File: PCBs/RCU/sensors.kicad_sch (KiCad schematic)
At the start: 11 parts, among them U501 LSM6DS3

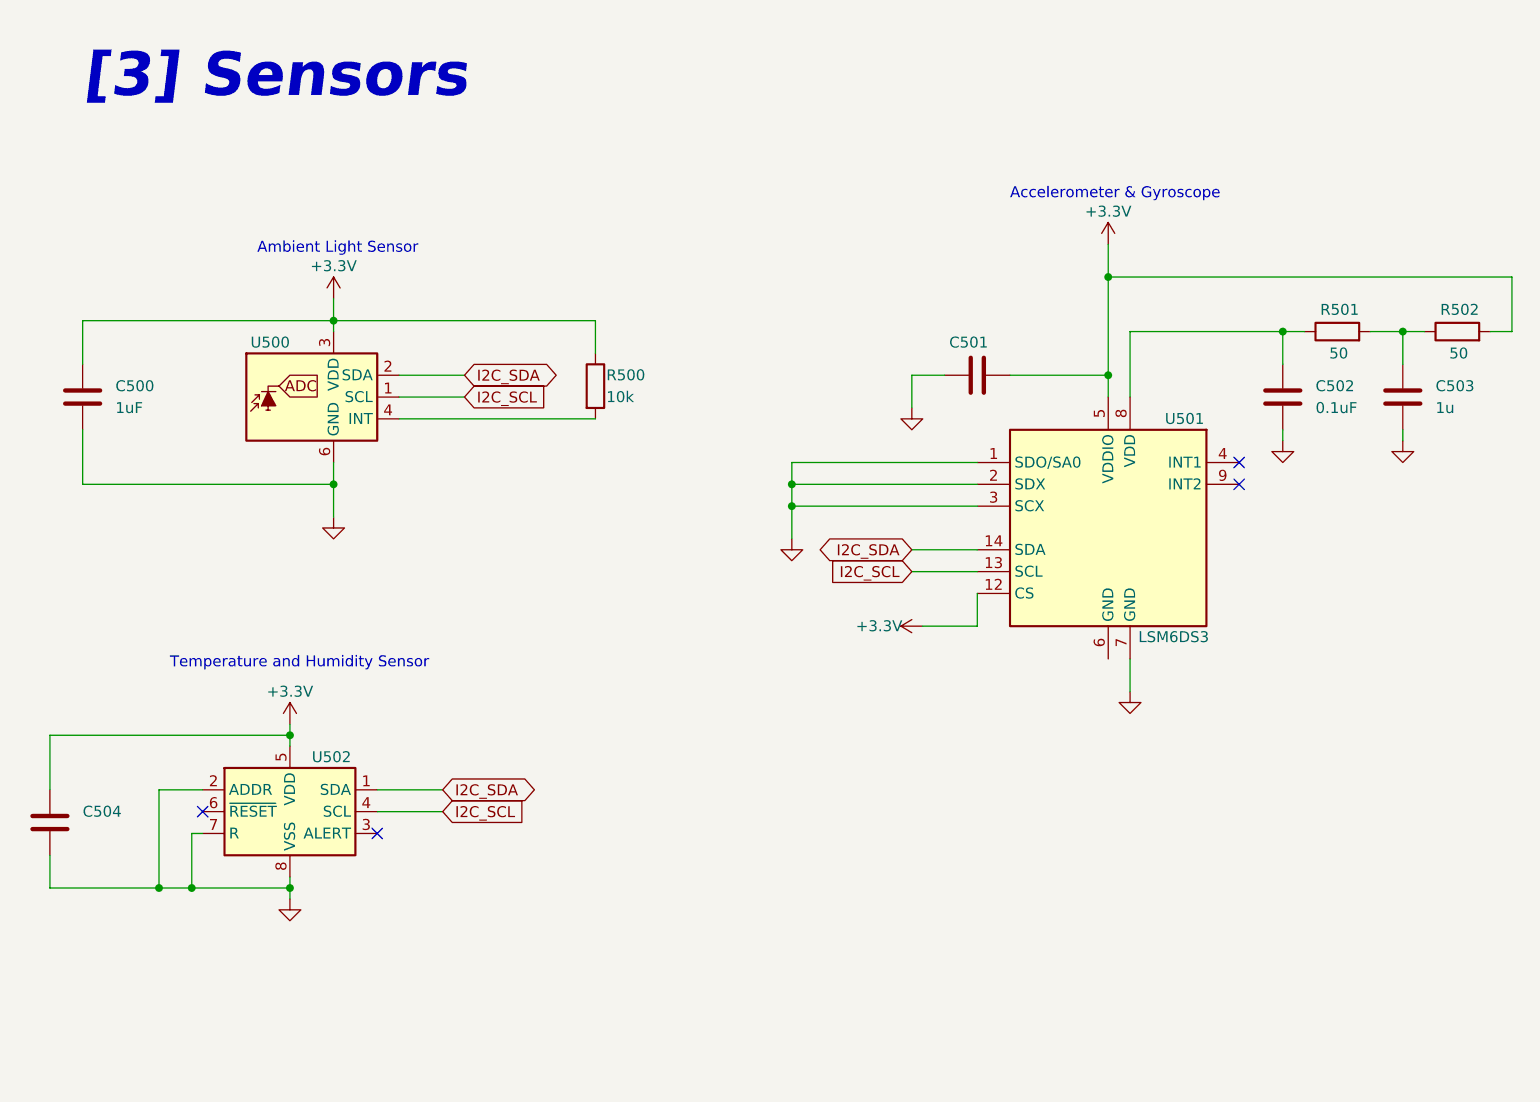
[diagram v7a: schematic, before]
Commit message: Sectioned ADC module and corrected Motor current output name
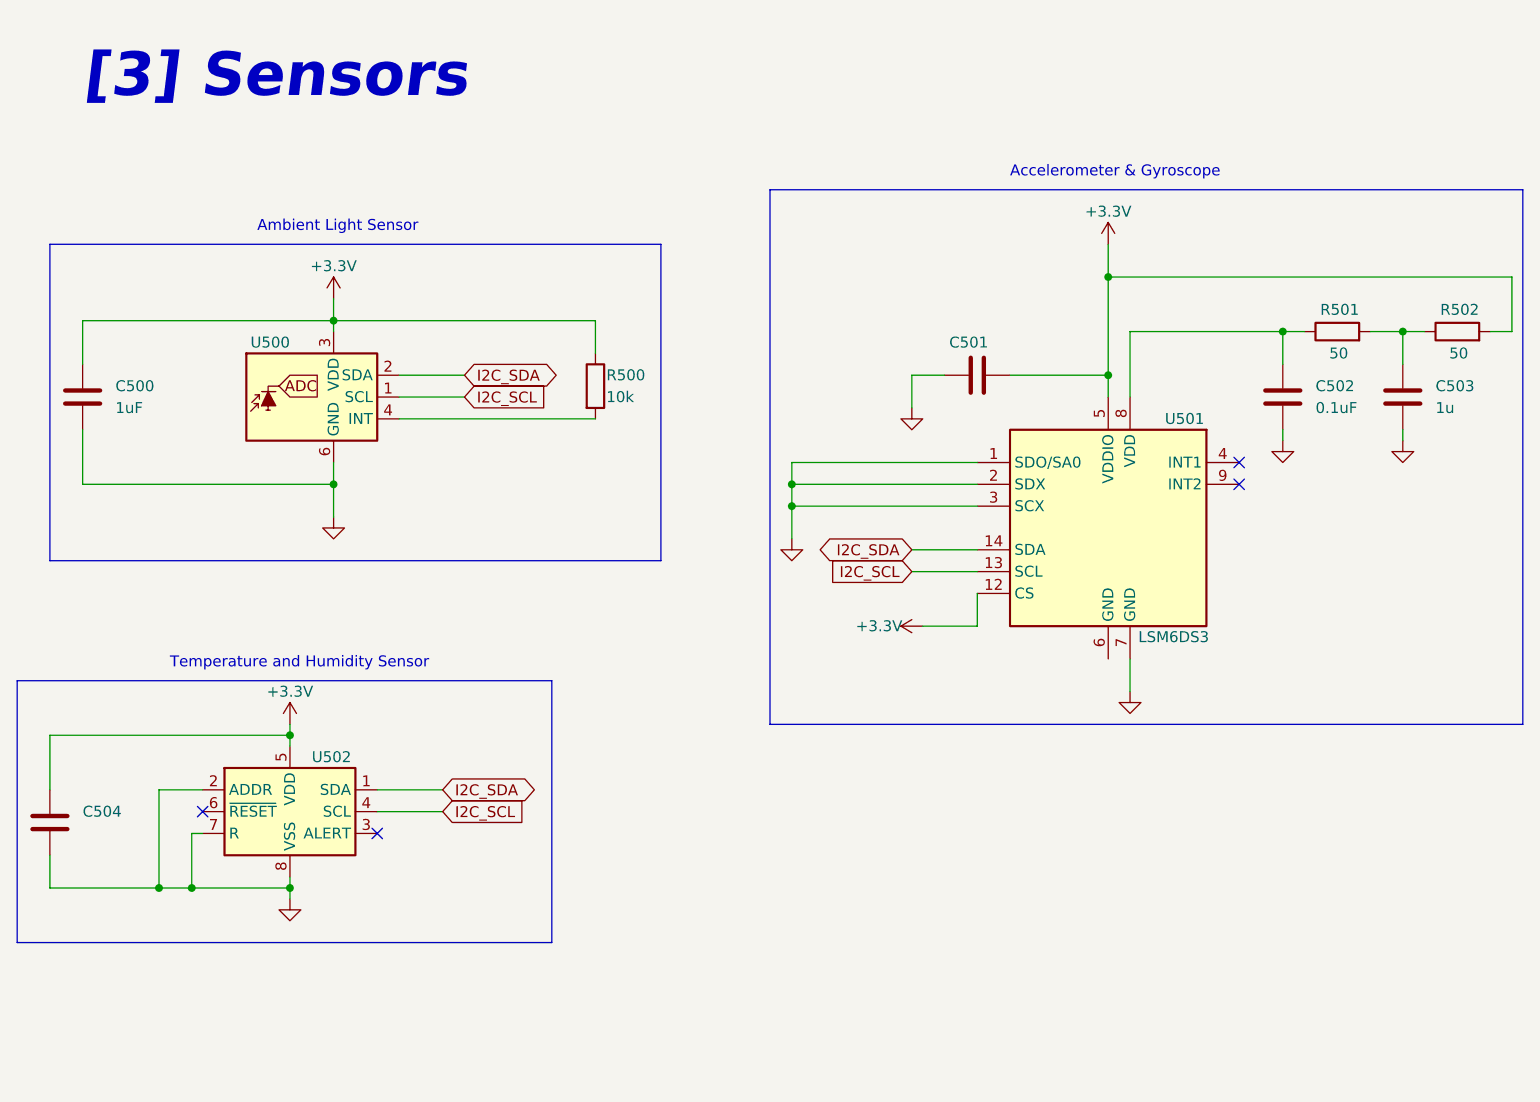
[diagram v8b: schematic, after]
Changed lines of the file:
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@@
+    (stroke (width 0) (type default) (color 0 0 0 0))
+  )
+  (polyline (pts (xy 88.9 81.28) (xy 88.9 44.45))
     (stroke (width 0) (type default) (color 0 0 0 0))
   )
@@
     (stroke (width 0) (type default) (color 0 0 0 0))
   )
+  (polyline (pts (xy 13.97 125.73) (xy 13.97 95.25))
+    (stroke (width 0) (type default) (color 0 0 0 0))
+  )
+  (polyline (pts (xy 76.2 125.73) (xy 13.97 125.73))
+    (stroke (width 0) (type default) (color 0 0 0 0))
+  )
+  (polyline (pts (xy 88.9 44.45) (xy 17.78 44.45))
+    (stroke (width 0) (type default) (color 0 0 0 0))
+  )
   (wire (pts (xy 125.73 80.01) (xy 118.11 80.01))
     (stroke (width 0) (type default) (color 0 0 0 0))
@@
     (stroke (width 0) (type default) (color 0 0 0 0))
   )
+  (polyline (pts (xy 17.78 44.45) (xy 17.78 81.28))
+    (stroke (width 0) (type default) (color 0 0 0 0))
+  )
+  (polyline (pts (xy 189.23 38.1) (xy 189.23 100.33))
+    (stroke (width 0) (type default) (color 0 0 0 0))
+  )
   (wire (pts (xy 187.96 54.61) (xy 187.96 48.26))
     (stroke (width 0) (type default) (color 0 0 0 0))
@@
     (stroke (width 0) (type default) (color 0 0 0 0))
   )
+  (polyline (pts (xy 101.6 100.33) (xy 101.6 38.1))
+    (stroke (width 0) (type default) (color 0 0 0 0))
+  )
   (wire (pts (xy 185.42 54.61) (xy 187.96 54.61))
     (stroke (width 0) (type default) (color 0 0 0 0))
@@
     (stroke (width 0) (type default) (color 0 0 0 0))
   )
+  (polyline (pts (xy 17.78 81.28) (xy 88.9 81.28))
+    (stroke (width 0) (type default) (color 0 0 0 0))
+  )
   (wire (pts (xy 118.11 59.69) (xy 121.92 59.69))
     (stroke (width 0) (type default) (color 0 0 0 0))
   )
+  (polyline (pts (xy 76.2 95.25) (xy 76.2 125.73))
+    (stroke (width 0) (type default) (color 0 0 0 0))
+  )
   (wire (pts (xy 118.11 59.69) (xy 118.11 63.5))
     (stroke (width 0) (type default) (color 0 0 0 0))
   )
+  (polyline (pts (xy 101.6 38.1) (xy 189.23 38.1))
+    (stroke (width 0) (type default) (color 0 0 0 0))
+  )
   (wire (pts (xy 45.72 100.33) (xy 45.72 101.6))
     (stroke (width 0) (type default) (color 0 0 0 0))
@@
     (stroke (width 0) (type default) (color 0 0 0 0))
   )
+  (polyline (pts (xy 189.23 100.33) (xy 101.6 100.33))
+    (stroke (width 0) (type default) (color 0 0 0 0))
+  )
   (wire (pts (xy 140.97 59.69) (xy 129.54 59.69))
     (stroke (width 0) (type default) (color 0 0 0 0))
@@
   )
   (wire (pts (xy 50.8 69.85) (xy 50.8 72.39))
+    (stroke (width 0) (type default) (color 0 0 0 0))
+  )
+  (polyline (pts (xy 13.97 95.25) (xy 76.2 95.25))
     (stroke (width 0) (type default) (color 0 0 0 0))
   )
@@
     (effects (font (size 5.08 5.08) (thickness 1.016) bold italic) (justify left bottom))
   )
-  (text "Accelerometer & Gyroscope" (at 129.54 39.37 0)
+  (text "Accelerometer & Gyroscope" (at 129.54 36.83 0)
     (effects (font (size 1.27 1.27)) (justify left bottom))
   )
-  (text "Ambient Light Sensor" (at 41.91 45.72 0)
+  (text "Ambient Light Sensor" (at 41.91 43.18 0)
     (effects (font (size 1.27 1.27)) (justify left bottom))
   )
